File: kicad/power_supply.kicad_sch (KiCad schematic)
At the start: 18 parts, among them J5 Conn_01x02, U5 ISL85410FRZ-T7A

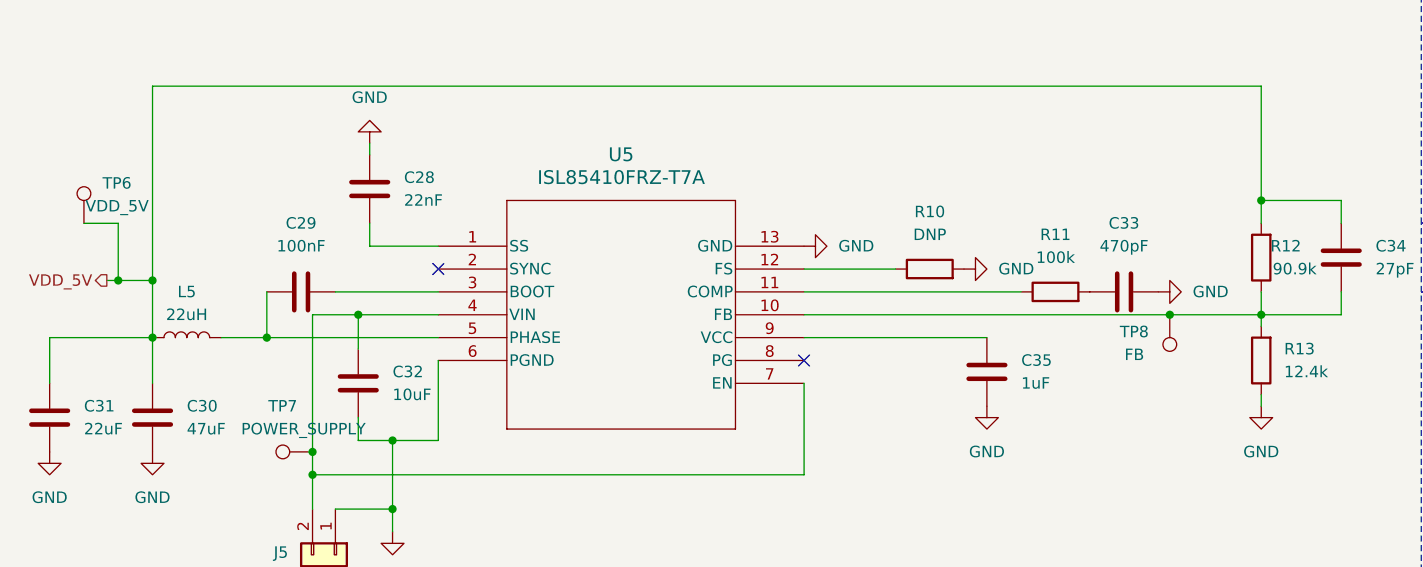
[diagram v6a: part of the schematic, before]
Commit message: feat(PCB): set component-placement example on PCB
This pr will fail due to DRC, skip this and lets have a conversation
about the placement only

Signed-off-by: Bobo Bäck Engström <bobo@id8-engineering.io>
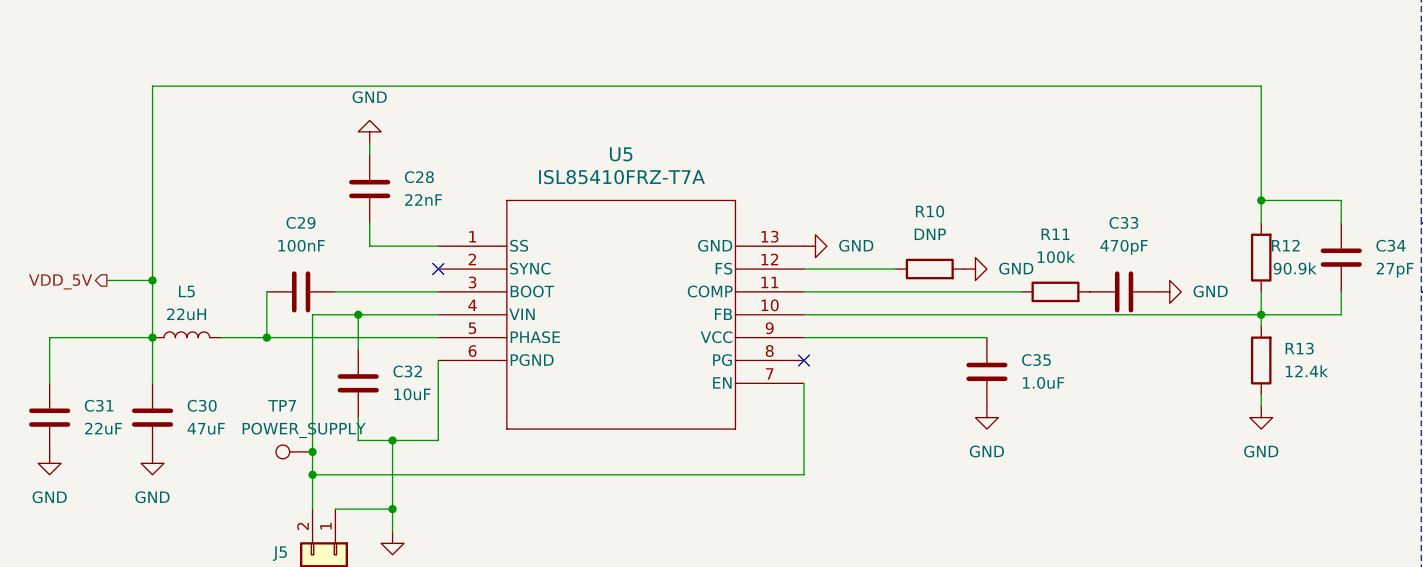
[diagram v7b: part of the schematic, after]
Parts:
- removed TP6: VDD_5V, seven-lib:TestPoint_Pad_2.0x2.0mm, symbol seven_lib:TestPoint
- removed TP8: FB, seven-lib:TestPoint_Pad_2.0x2.0mm, symbol seven_lib:TestPoint
- C28: MPN (none) -> GRM155R71C223KA01D
- C29: MPN (none) -> GRM155R71C104KA88D
- C30: footprint seven-lib:C_0402_1005Metric -> seven-lib:C_0805_2012Metric; MPN (none) -> GRM21BC8YA476ME11L
- C31: footprint seven-lib:C_0402_1005Metric -> seven-lib:C_0805_2012Metric; MPN (none) -> GRM21BR60J226ME39L
- C32: footprint seven-lib:C_0402_1005Metric -> seven-lib:C_0805_2012Metric; MPN (none) -> GRM21BR61A106KE51L
- C33: MPN (none) -> GRM1555C1H471JA01D
- C34: MPN (none) -> GRM1555C1H270JA01D
- C35: value 1uF -> 1.0uF; footprint seven-lib:C_0402_1005Metric -> seven-lib:C_0603_1608Metric; MPN (none) -> GRM188R71C105KA12D
- J5: LCSC (none) -> C2915639; MPN (none) -> 1757242
- L5: footprint seven-lib:L_0603_1608Metric -> seven-lib:L_1008_2520Metric; MPN (none) -> LQH2HPN220MGRL
- R11: MPN (none) -> RC0402FR-07100KL
- R12: MPN (none) -> RC0402FR-0790K9L
- R13: MPN (none) -> RC0402FR-0712K4L
- U5: MPN (none) -> ISL85410FRZ-T7A

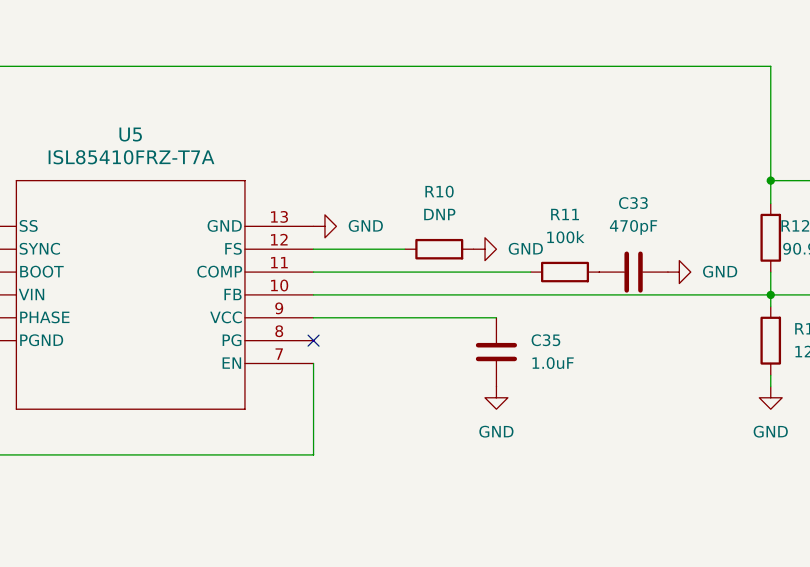
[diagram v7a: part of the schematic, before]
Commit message: fix: fix issues from seven prototype 1
see https://github.com/id8-engineering/seven-bringup/issues/22

Signed-off-by: Bobo Bäck Engström <bobo@id8-engineering.io>
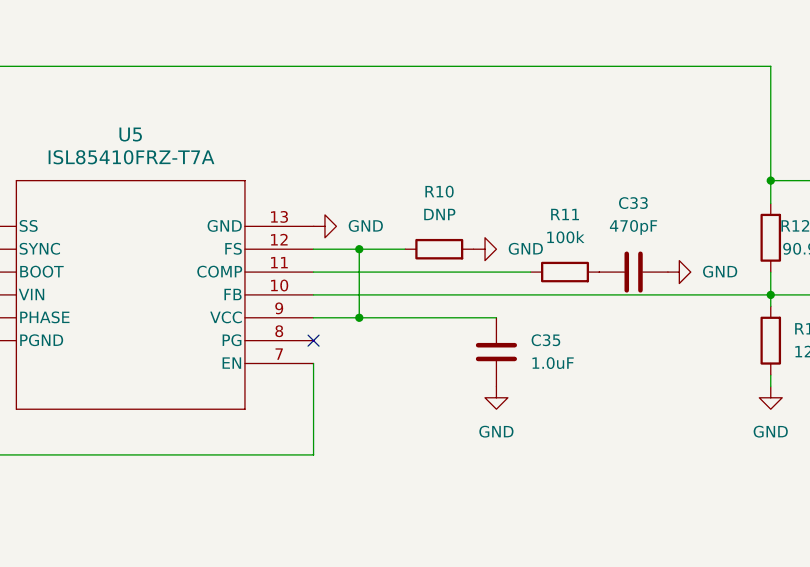
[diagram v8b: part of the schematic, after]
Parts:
- C30: MPN GRM21BC8YA476ME11L -> CL21A476MQYNNNE
- C32: MPN GRM21BR61A106KE51L -> CL21A106KAYNNNE
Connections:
- net at R10.1, U5.12 (FS): now also C35.2, U5.9 (VCC)
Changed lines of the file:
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@@
+	)
+	(junction
+		(at 113.03 82.55)
+		(diameter 0)
+		(color 0 0 0 0)
 	)
 	(junction
@@
 	)
 	(junction
+		(at 113.03 90.17)
+		(diameter 0)
+		(color 0 0 0 0)
+	)
+	(junction
 		(at 158.75 74.93)
 		(diameter 0)
@@
 	(wire
 		(pts
+			(xy 113.03 82.55) (xy 113.03 90.17)
+		)
+		(stroke
+			(width 0)
+			(type default)
+		)
+	)
+	(wire
+		(pts
 			(xy 107.95 105.41) (xy 107.95 95.25)
 		)
@@
 	(wire
 		(pts
-			(xy 107.95 82.55) (xy 118.11 82.55)
+			(xy 107.95 82.55) (xy 113.03 82.55)
 		)
 		(stroke
@@
 	(wire
 		(pts
+			(xy 113.03 90.17) (xy 128.27 90.17)
+		)
+		(stroke
+			(width 0)
+			(type default)
+		)
+	)
+	(wire
+		(pts
 			(xy 167.64 74.93) (xy 167.64 77.47)
 		)
@@
 	(wire
 		(pts
-			(xy 128.27 90.17) (xy 107.95 90.17)
+			(xy 107.95 90.17) (xy 113.03 90.17)
 		)
 		(stroke
@@
 		(pts
 			(xy 67.31 90.17) (xy 48.26 90.17)
+		)
+		(stroke
+			(width 0)
+			(type default)
+		)
+	)
+	(wire
+		(pts
+			(xy 113.03 82.55) (xy 118.11 82.55)
 		)
 		(stroke
@@
 			)
 		)
-		(property "MPN" "GRM21BR61A106KE51L"
+		(property "MPN" "CL21A106KAYNNNE"
 			(at 58.42 95.25 0)
 			(hide yes)
@@
 			)
 		)
-		(property "MPN" "GRM21BC8YA476ME11L"
+		(property "MPN" "CL21A476MQYNNNE"
 			(at 35.56 99.06 0)
 			(hide yes)
